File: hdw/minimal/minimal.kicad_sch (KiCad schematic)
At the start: 8 parts, among them J1 USB_A, U2 CH334U, Y1 12MHz

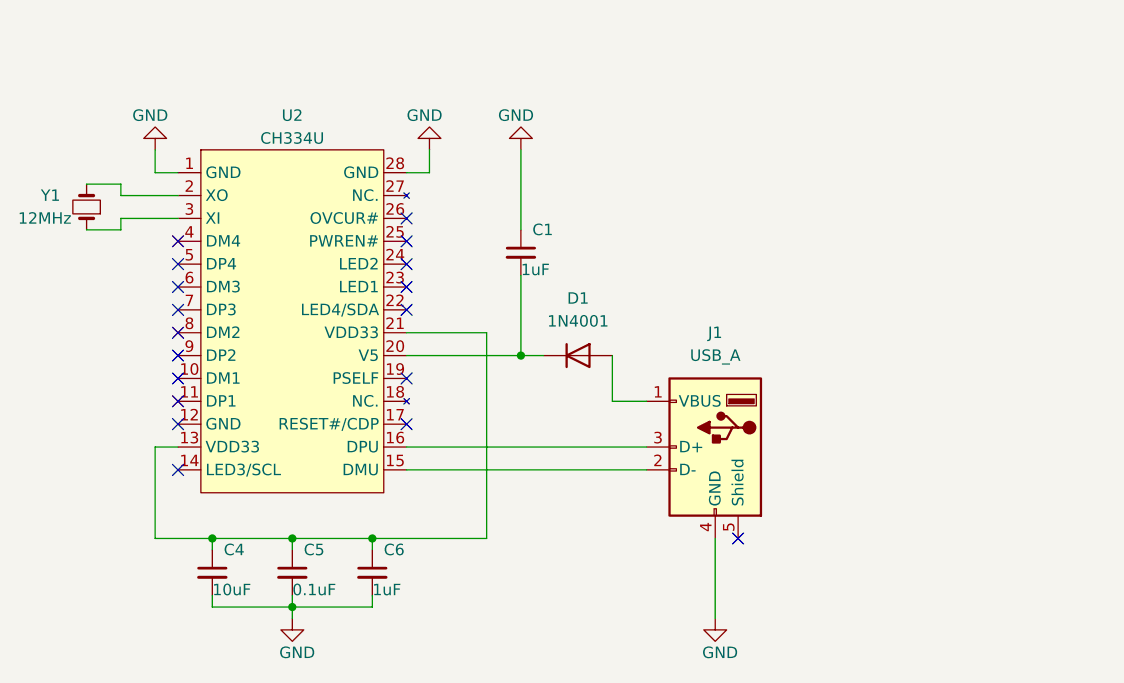
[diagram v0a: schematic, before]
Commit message: update schematic
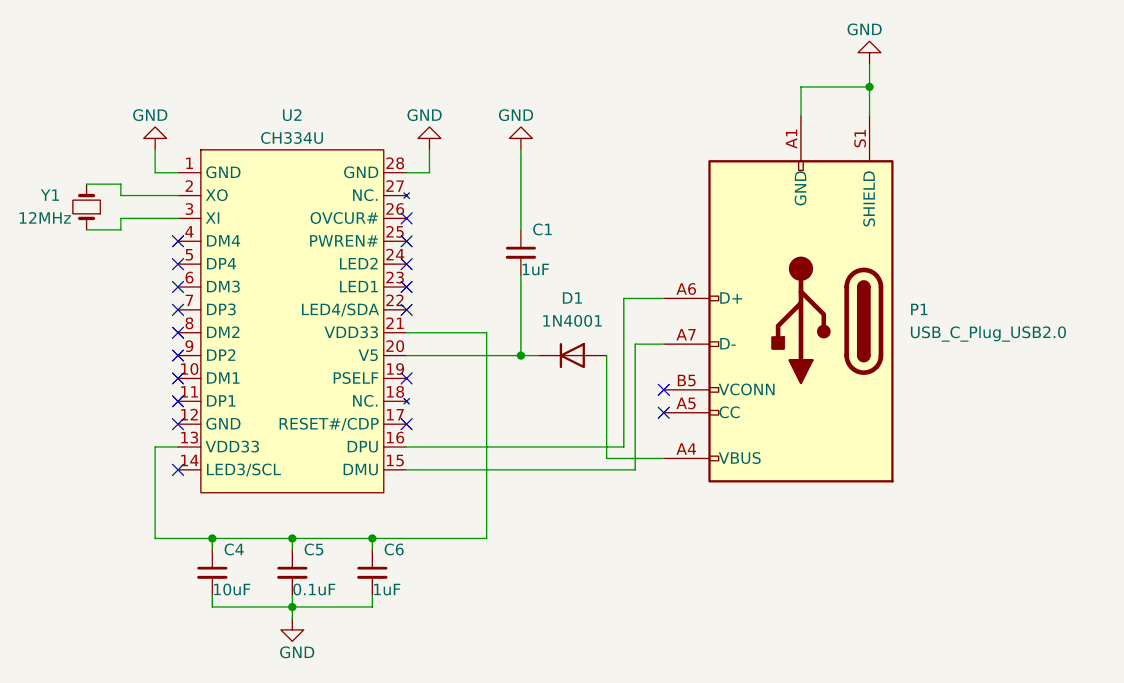
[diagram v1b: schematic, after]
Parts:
- removed J1: USB_A, symbol Connector:USB_A
- added P1: USB_C_Plug_USB2.0, symbol Connector:USB_C_Plug_USB2.0
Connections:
- net GND: now also P1.A1 (GND), P1.A12 (GND), P1.B1 (GND), P1.B12 (GND), P1.S1 (SHIELD)
- net at D1.2 (A): now also P1.A4 (VBUS), P1.A9 (VBUS), P1.B4 (VBUS), P1.B9 (VBUS)
- net at U2.15 (DMU): now also P1.A7 (D-)
- net at U2.16 (DPU): now also P1.A6 (D+)
- no-connect marks 18 -> 19
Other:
- moved on the sheet: D1
